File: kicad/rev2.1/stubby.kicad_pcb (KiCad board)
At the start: 2 copper layers, 49.5 x 49.5 mm, 74 parts, among them IC1 ATMEGA1284-A, P1 CONN_6, P10 CONN_4, P11 CONN_6, P2 CONN_4, P3 CONN_13, P4 CONN_2, P5 CONN_1, P6 CONN_6, P7 CONN_10, P8 BATT (4.8V-6V), P9 PROG, SW1 SW_PUSH, SW2 DPDT, U1 HMC5883L, X1 20MHz

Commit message: More routing of power supply
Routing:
- net GND: track 202.6 -> 202.0 mm
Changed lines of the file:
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@@
     (thickness 1.6)
     (drawings 79)
-    (tracks 839)
+    (tracks 840)
     (zones 0)
     (modules 74)
@@
   (segment (start 36.83 28.575) (end 36.322 28.194) (width 0.254) (layer B.Cu) (net 6) (status 30))
   (segment (start 36.83 28.702) (end 36.322 28.194) (width 0.254) (layer B.Cu) (net 6) (status 20))
-  (segment (start 64.262 33.655) (end 64.77 33.655) (width 0.254) (layer F.Cu) (net 7))
+  (segment (start 64.262 33.655) (end 65.405 33.655) (width 0.254) (layer F.Cu) (net 7))
+  (segment (start 66.04 33.02) (end 66.04 32.385) (width 0.254) (layer F.Cu) (net 7))
+  (segment (start 65.405 33.655) (end 66.04 33.02) (width 0.254) (layer F.Cu) (net 7))
   (segment (start 66.04 32.385) (end 69.85 36.195) (width 0.254) (layer B.Cu) (net 7))
   (via (at 66.04 32.385) (size 0.762) (layers F.Cu B.Cu) (net 7))
-  (segment (start 64.77 33.655) (end 66.04 32.385) (width 0.254) (layer F.Cu) (net 7))
   (segment (start 68.53414 45.03914) (end 69.215 45.72) (width 0.254) (layer F.Cu) (net 7))
   (segment (start 69.215 45.72) (end 69.85 45.72) (width 0.254) (layer F.Cu) (net 7))
@@
   (segment (start 59.886153 37.441616) (end 59.055 36.610463) (width 0.254) (layer F.Cu) (net 14))
   (segment (start 59.055 36.195) (end 59.055 36.610463) (width 0.254) (layer F.Cu) (net 14))
-  (segment (start 64.262 29.845) (end 64.77 29.845) (width 0.254) (layer F.Cu) (net 15))
-  (segment (start 67.83 27.19) (end 67.08 27.19) (width 0.254) (layer F.Cu) (net 15))
-  (segment (start 68.58 27.94) (end 67.83 27.19) (width 0.254) (layer F.Cu) (net 15))
-  (segment (start 68.58 29.845) (end 68.58 27.94) (width 0.254) (layer F.Cu) (net 15))
+  (segment (start 67.08 27.19) (end 68.338 27.19) (width 0.254) (layer F.Cu) (net 15))
+  (segment (start 68.58 27.432) (end 68.58 29.845) (width 0.254) (layer F.Cu) (net 15))
+  (segment (start 68.338 27.19) (end 68.58 27.432) (width 0.254) (layer F.Cu) (net 15))
+  (segment (start 64.262 29.845) (end 65.405 29.845) (width 0.254) (layer F.Cu) (net 15))
+  (segment (start 65.405 29.845) (end 66.04 30.48) (width 0.254) (layer F.Cu) (net 15))
   (segment (start 67.945 30.48) (end 68.58 29.845) (width 0.254) (layer F.Cu) (net 15))
-  (segment (start 65.405 30.48) (end 67.945 30.48) (width 0.254) (layer F.Cu) (net 15))
-  (segment (start 64.77 29.845) (end 65.405 30.48) (width 0.254) (layer F.Cu) (net 15))
+  (segment (start 66.04 30.48) (end 67.945 30.48) (width 0.254) (layer F.Cu) (net 15))
   (segment (start 58.42 33.02) (end 61.595 29.845) (width 0.254) (layer F.Cu) (net 16))
   (segment (start 61.595 29.845) (end 61.595 29.21) (width 0.254) (layer F.Cu) (net 16))
@@
   (segment (start 58.42 37.106975) (end 59.320397 38.007372) (width 0.254) (layer F.Cu) (net 16))
   (segment (start 58.42 37.106975) (end 58.42 37.106975) (width 0.254) (layer F.Cu) (net 16))
-  (segment (start 64.262 27.94) (end 64.77 27.94) (width 0.254) (layer F.Cu) (net 17))
-  (segment (start 65.52 28.69) (end 67.08 28.69) (width 0.254) (layer F.Cu) (net 17))
-  (segment (start 64.77 27.94) (end 65.52 28.69) (width 0.254) (layer F.Cu) (net 17))
+  (segment (start 64.262 27.94) (end 65.405 27.94) (width 0.254) (layer F.Cu) (net 17))
+  (segment (start 66.155 28.69) (end 67.08 28.69) (width 0.254) (layer F.Cu) (net 17))
+  (segment (start 65.405 27.94) (end 66.155 28.69) (width 0.254) (layer F.Cu) (net 17))
   (segment (start 59.69 34.29) (end 61.595 32.385) (width 0.254) (layer F.Cu) (net 18))
   (segment (start 61.595 32.385) (end 62.23 31.75) (width 0.254) (layer F.Cu) (net 18))
@@
   (segment (start 59.69 34.29) (end 59.69 36.113951) (width 0.254) (layer F.Cu) (net 18))
   (segment (start 62.23 31.75) (end 62.738 31.75) (width 0.254) (layer F.Cu) (net 18))
-  (segment (start 64.262 31.75) (end 64.77 31.75) (width 0.254) (layer F.Cu) (net 19))
+  (segment (start 64.262 31.75) (end 65.405 31.75) (width 0.254) (layer F.Cu) (net 19))
+  (segment (start 65.405 31.75) (end 66.04 31.115) (width 0.254) (layer F.Cu) (net 19))
   (segment (start 70.08 28.98) (end 70.08 28.69) (width 0.254) (layer F.Cu) (net 19))
   (segment (start 67.945 31.115) (end 70.08 28.98) (width 0.254) (layer F.Cu) (net 19))
-  (segment (start 65.405 31.115) (end 67.945 31.115) (width 0.254) (layer F.Cu) (net 19))
-  (segment (start 64.77 31.75) (end 65.405 31.115) (width 0.254) (layer F.Cu) (net 19))
+  (segment (start 66.04 31.115) (end 67.945 31.115) (width 0.254) (layer F.Cu) (net 19))
   (segment (start 62.738 55.118) (end 63.627 55.118) (width 0.254) (layer B.Cu) (net 20))
   (segment (start 64.135 48.768) (end 63.119 47.752) (width 0.254) (layer B.Cu) (net 20))
@@
   (segment (start 63.119 48.595049) (end 64.008091 49.48414) (width 0.254) (layer F.Cu) (net 20))
   (via (at 63.119 47.752) (size 0.762) (layers F.Cu B.Cu) (net 20))
+  (segment (start 62.738 33.655) (end 61.595 33.655) (width 0.254) (layer F.Cu) (net 21))
+  (segment (start 60.96 34.29) (end 60.96 34.925) (width 0.254) (layer F.Cu) (net 21))
+  (segment (start 61.595 33.655) (end 60.96 34.29) (width 0.254) (layer F.Cu) (net 21))
   (segment (start 51.435 35.56) (end 52.705 35.56) (width 0.254) (layer B.Cu) (net 21))
   (segment (start 52.705 35.56) (end 53.34 34.925) (width 0.254) (layer F.Cu) (net 21))
@@
   (via (at 56.515 34.925) (size 0.762) (layers F.Cu B.Cu) (net 21))
   (segment (start 53.34 34.925) (end 56.515 34.925) (width 0.254) (layer F.Cu) (net 21))
-  (segment (start 60.96 34.925) (end 62.23 33.655) (width 0.254) (layer F.Cu) (net 21))
   (via (at 60.96 34.925) (size 0.762) (layers F.Cu B.Cu) (net 21))
   (segment (start 60.96 34.925) (end 56.515 34.925) (width 0.254) (layer B.Cu) (net 21))
-  (segment (start 62.23 33.655) (end 62.738 33.655) (width 0.254) (layer F.Cu) (net 21))
   (segment (start 48.26 41.91) (end 48.26 38.735) (width 0.254) (layer B.Cu) (net 21))
   (segment (start 48.26 38.735) (end 51.435 35.56) (width 0.254) (layer B.Cu) (net 21))
@@
   (segment (start 71.755 47.085) (end 74.263 47.085) (width 0.254) (layer F.Cu) (net 45))
   (segment (start 74.263 47.085) (end 74.295 47.117) (width 0.254) (layer F.Cu) (net 45))
+  (segment (start 59.817 25.4) (end 59.817 24.257) (width 0.254) (layer F.Cu) (net 46))
+  (via (at 59.69 24.13) (size 0.762) (layers F.Cu B.Cu) (net 46))
+  (segment (start 59.817 24.257) (end 59.69 24.13) (width 0.254) (layer F.Cu) (net 46))
+  (segment (start 59.817 25.4) (end 60.96 25.4) (width 0.254) (layer F.Cu) (net 46))
+  (segment (start 53.0225 24.765) (end 53.0225 25.7175) (width 0.254) (layer F.Cu) (net 46))
+  (via (at 53.34 26.035) (size 0.762) (layers F.Cu B.Cu) (net 46))
+  (segment (start 53.0225 25.7175) (end 53.34 26.035) (width 0.254) (layer F.Cu) (net 46))
   (segment (start 54.102 33.655) (end 54.102 33.528) (width 0.254) (layer F.Cu) (net 46))
   (via (at 54.61 33.02) (size 0.762) (layers F.Cu B.Cu) (net 46))
@@
   (via (at 57.785 29.845) (size 0.762) (layers F.Cu B.Cu) (net 46))
   (segment (start 57.95518 29.67482) (end 57.785 29.845) (width 0.254) (layer F.Cu) (net 46))
-  (segment (start 62.23 24.638) (end 60.452 24.638) (width 0.254) (layer F.Cu) (net 46))
-  (segment (start 59.817 25.273) (end 60.325 24.765) (width 0.254) (layer F.Cu) (net 46))
-  (via (at 60.325 24.765) (size 0.762) (layers F.Cu B.Cu) (net 46))
-  (segment (start 59.817 25.273) (end 59.817 25.4) (width 0.254) (layer F.Cu) (net 46))
-  (segment (start 60.452 24.638) (end 60.325 24.765) (width 0.254) (layer F.Cu) (net 46))
   (segment (start 54.102 33.655) (end 56.388 33.655) (width 0.254) (layer F.Cu) (net 46))
   (segment (start 56.388 33.655) (end 56.515 33.528) (width 0.254) (layer F.Cu) (net 46))
-  (segment (start 53.0225 24.765) (end 53.0225 25.0825) (width 0.254) (layer F.Cu) (net 46))
-  (via (at 52.07 26.035) (size 0.762) (layers F.Cu B.Cu) (net 46))
-  (segment (start 53.0225 25.0825) (end 52.07 26.035) (width 0.254) (layer F.Cu) (net 46))
   (segment (start 54.9275 25.4) (end 54.9275 27.94) (width 0.508) (layer F.Cu) (net 46))
   (segment (start 54.9275 27.94) (end 54.9275 29.7815) (width 0.508) (layer F.Cu) (net 46))

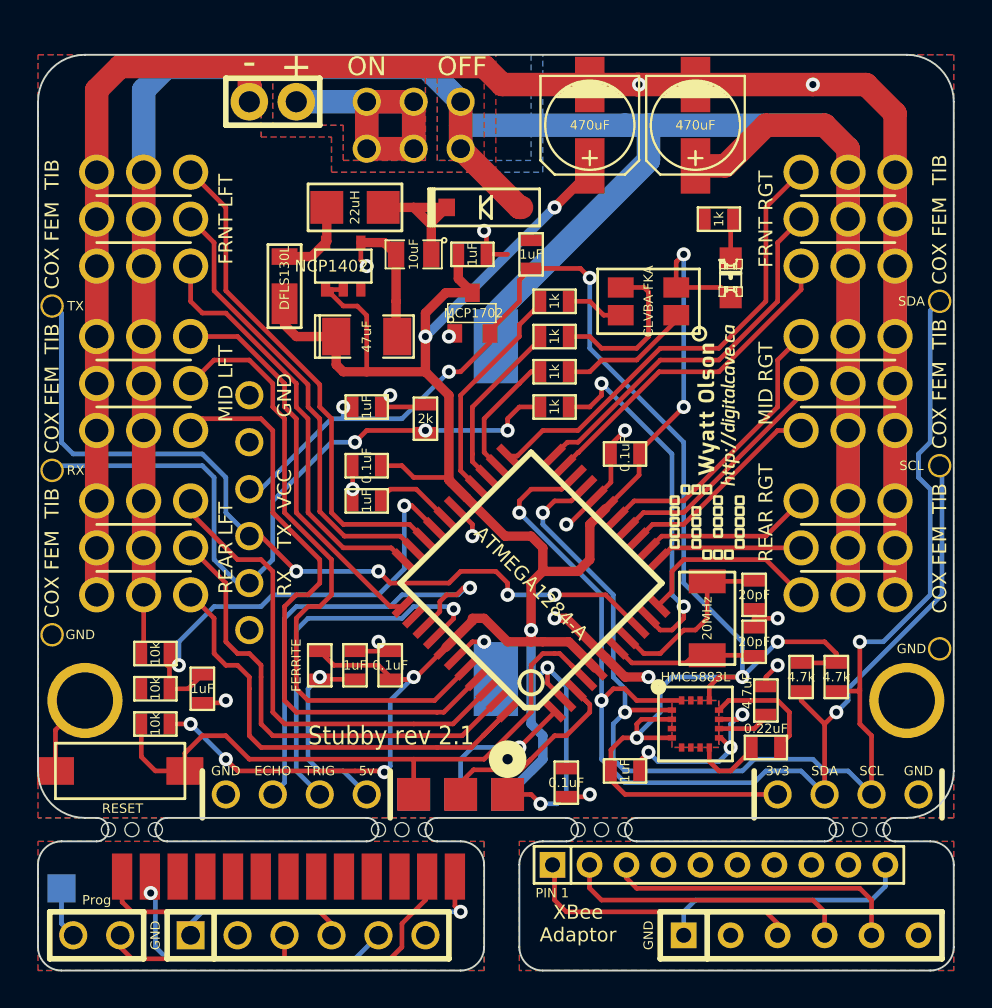
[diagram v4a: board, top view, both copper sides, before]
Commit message: working on heat dissipation for ncp1402
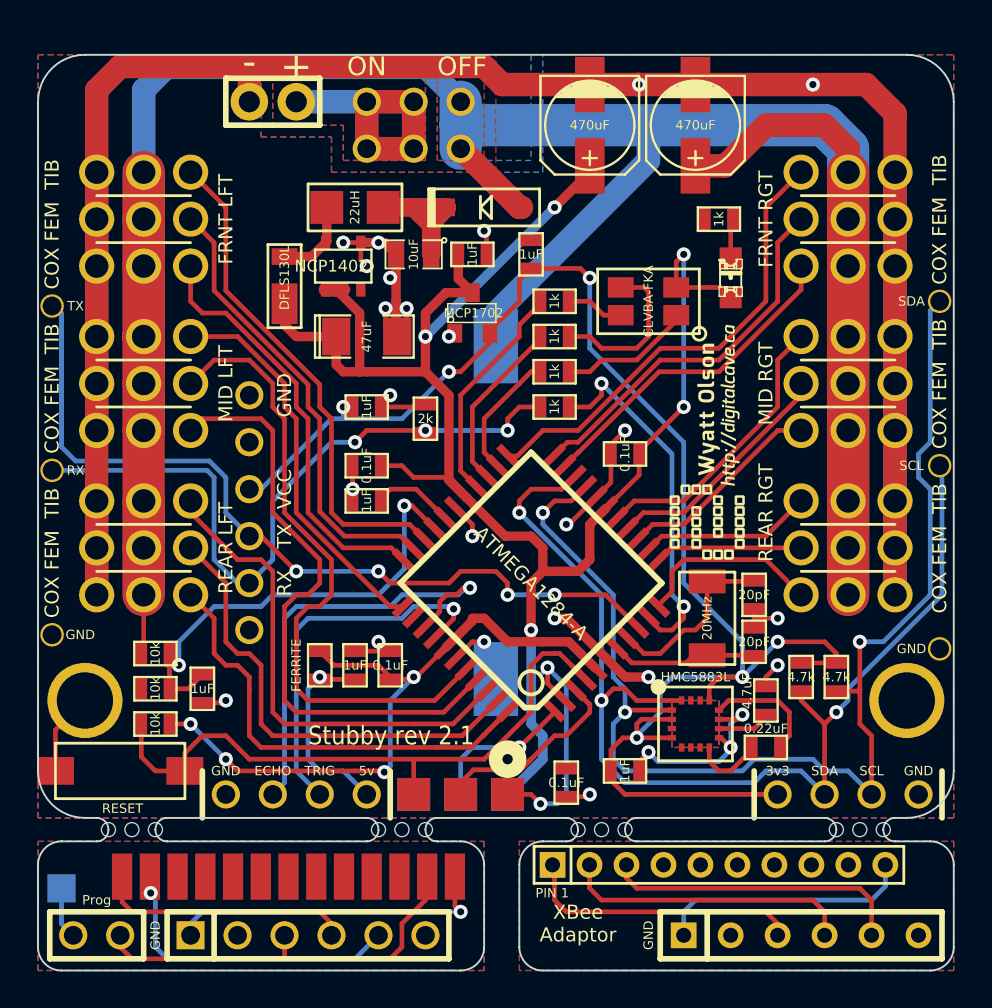
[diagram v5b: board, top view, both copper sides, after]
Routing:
- net +BATT: track 172.6 -> 199.1 mm
- net GND: track 202.0 -> 209.6 mm, vias 21 -> 26
- net +5V: track 139.0 -> 138.3 mm
